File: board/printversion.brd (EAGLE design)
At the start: 70.3 x 34.5 mm, 36 parts, among them IC1 TPS61070DDC, IC2 MEGA8-P, Q2 16MHz

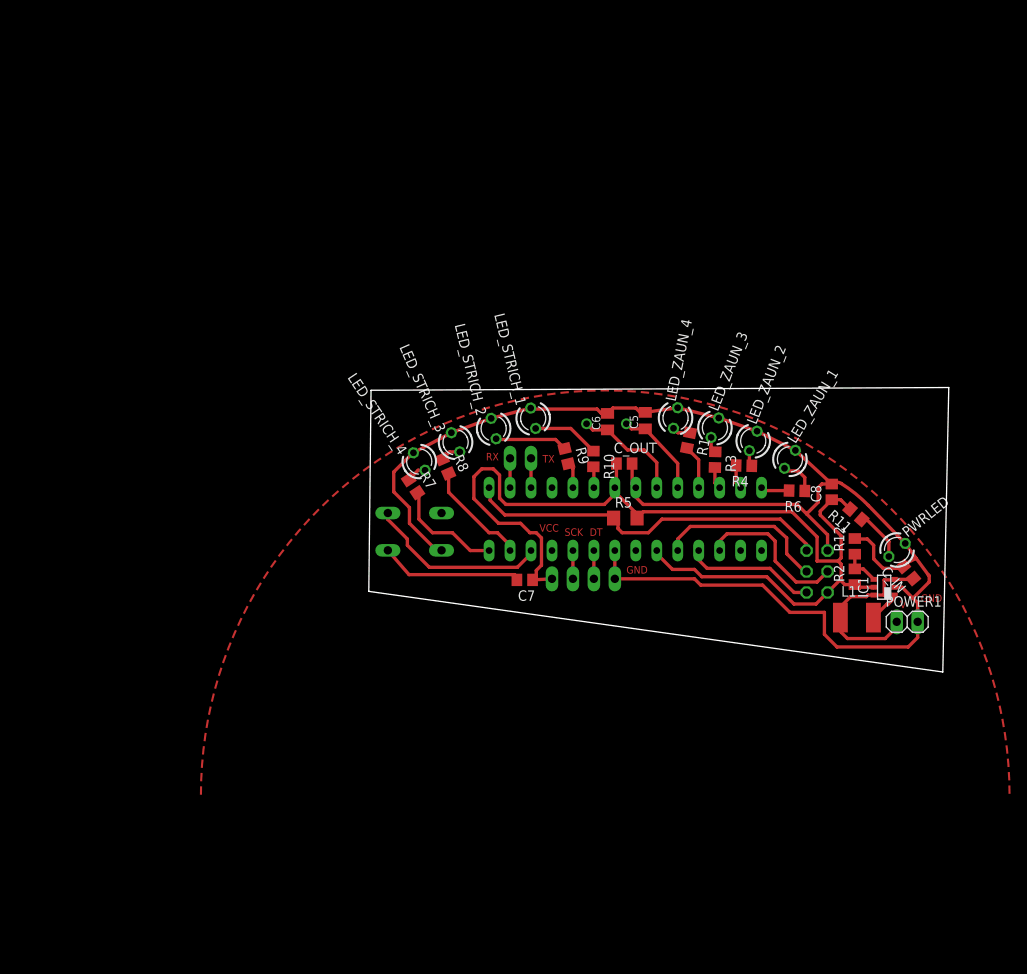
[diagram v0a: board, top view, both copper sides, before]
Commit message: added printversion with multiple boards per page
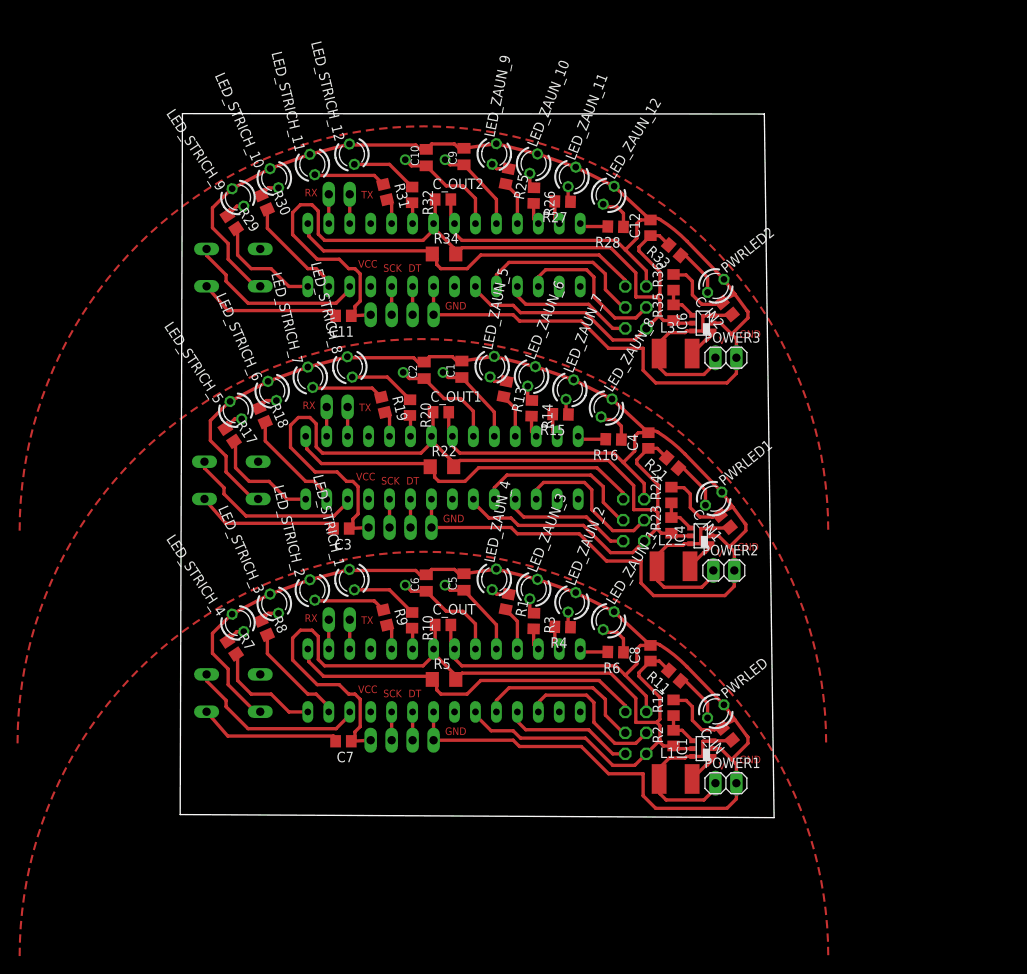
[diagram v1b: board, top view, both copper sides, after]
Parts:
- added C1, C10, C2, C9: 18pF, resistor:C0805K
- added C11, C3: 1uF, rcl-2:C0805
- added C12, C4: 100n, rcl-2:C0805
- added C_IN1, C_IN2, C_OUT1, C_OUT2: (no value), rcl-2:C0805
- added HX2, HX3: JP1, pinhead:1X04
- added IC3, IC5: MEGA8-P, atmel:DIL28-3
- added IC4, IC6: TPS61070DDC, texas:TSOT23-6_DDC
- added ISP2, ISP3: ISP-Connector, con-panduit:057-006-1
- added L2, L3: (no value), rcl:L4532P
- added LED_STRICH_10, LED_STRICH_11, LED_STRICH_12, LED_STRICH_5, LED_STRICH_6, LED_STRICH_7, LED_STRICH_8, LED_STRICH_9, LED_ZAUN_10, LED_ZAUN_11, LED_ZAUN_12, LED_ZAUN_5, LED_ZAUN_6, LED_ZAUN_7, LED_ZAUN_8, LED_ZAUN_9, PWRLED1, PWRLED2: (no value), led:LED3MM
- added POWER2, POWER3, UART2, UART3: JP2, pinhead:1X02
- added Q1, Q3: 16MHz, crystal:HC49/S
- added R13, R14, R15, R16, R17, R18, R19, R20, R21, R25, R26, R27, R28, R29, R30, R31, R32, R33: 470, resistor:R0805
- added R22, R34: 10k, rcl-2:R1206
- added R23, R24, R35, R36: (no value), resistor:R0805
- added S1, S3: S1, switch-omron:B3F-10XX
- moved C6 29.4 mm to (27.3, 25.7)
- moved C7 29.4 mm to (17.3, 6.48)
- moved IC1 29.4 mm to (60.8, 5.59)
- moved IC2 29.4 mm to (29.5, 13.8)
- moved ISP1 29.4 mm to (52.7, 7.49)
- moved PWRLED 29.4 mm to (62.4, 10.1)
- moved R11 29.4 mm to (57.4, 14.4)
- moved R12 29.4 mm to (57.3, 10.5)
- moved R2 29.4 mm to (57.3, 6.86)
- moved R5 29.4 mm to (29.5, 14.0)
- moved R8 29.4 mm to (7.67, 20.2)
- moved C5 29.4 mm to (31.9, 25.8)
- moved C8 29.4 mm to (54.5, 17.1)
- moved LED_STRICH_1 29.4 mm to (18.3, 26.1)
- moved LED_STRICH_3 29.4 mm to (8.89, 23.2)
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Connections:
- new net +5V1: C3.1, C4.1, C_OUT1.1, HX2.4, IC3.20, IC3.7, IC4.5, ISP2.2, R21.2, R22.2, R23.1
- new net +5V2: C11.1, C12.1, C_OUT2.1, HX3.4, IC5.20, IC5.7, IC6.5, ISP3.2, R33.2, R34.2, R35.1
- new net GND1: C1.2, C2.2, C4.2, C_IN1.2, C_OUT1.2, HX2.1, IC3.22, IC3.8, IC4.2, ISP2.6, LED_STRICH_5.K, LED_STRICH_6.K, LED_STRICH_7.K, LED_STRICH_8.K, LED_ZAUN_5.K, LED_ZAUN_6.K, LED_ZAUN_7.K, LED_ZAUN_8.K, POWER2.2, PWRLED1.K, R24.2, S1.3
- new net GND2: C10.2, C12.2, C9.2, C_IN2.2, C_OUT2.2, HX3.1, IC5.22, IC5.8, IC6.2, ISP3.6, LED_STRICH_10.K, LED_STRICH_11.K, LED_STRICH_12.K, LED_STRICH_9.K, LED_ZAUN_10.K, LED_ZAUN_11.K, LED_ZAUN_12.K, LED_ZAUN_9.K, POWER3.2, PWRLED2.K, R36.2, S3.3
- new net N$16: LED_ZAUN_5.A, R13.1
- new net N$17: LED_ZAUN_6.A, R14.1
- new net N$18: LED_ZAUN_7.A, R15.1
- new net N$19: LED_ZAUN_8.A, R16.1
- new net N$20: LED_STRICH_5.A, R17.1
- new net N$21: LED_STRICH_6.A, R18.1
- new net N$22: LED_STRICH_7.A, R19.1
- new net N$23: LED_STRICH_8.A, R20.1
- new net N$24: PWRLED1.A, R21.1
- new net N$25: C1.1, IC3.10, Q1.2
- new net N$26: C2.1, IC3.9, Q1.1
- new net N$27: C3.2, S1.4
- new net N$28: IC4.1, L2.2
- new net N$29: IC4.4, R23.2, R24.1
- new net N$31: LED_ZAUN_9.A, R25.1
- new net N$32: LED_ZAUN_10.A, R26.1
- new net N$33: LED_ZAUN_11.A, R27.1
- new net N$34: LED_ZAUN_12.A, R28.1
- new net N$35: LED_STRICH_9.A, R29.1
- new net N$36: LED_STRICH_10.A, R30.1
- new net N$37: LED_STRICH_11.A, R31.1
- new net N$38: LED_STRICH_12.A, R32.1
- new net N$39: PWRLED2.A, R33.1
- new net N$40: C9.1, IC5.10, Q3.2
- new net N$41: C10.1, IC5.9, Q3.1
- new net N$42: C11.2, S3.4
- new net N$43: IC6.1, L3.2
- new net N$44: IC6.4, R35.2, R36.1
- new net PB0/LED_ZAUN_2: IC3.14, R16.2
- new net PB0/LED_ZAUN_3: IC5.14, R28.2
- new net PB3: IC3.16
- new net PB3/MOSI1: IC3.17, ISP2.4
- new net PB3/MOSI2: IC5.17, ISP3.4
- new net PB4: IC3.15
- new net PB4/MISO1: IC3.18, ISP2.1
- new net PB4/MISO2: IC5.18, ISP3.1
- new net PB5: IC5.16
- new net PB5/SCK1: IC3.19, ISP2.3
- new net PB5/SCK2: IC5.19, ISP3.3
- new net PB6: IC5.15
- new net PC0/DT1: HX2.2, IC3.23
- new net PC0/DT2: HX3.2, IC5.23
- new net PC1: IC3.25
- new net PC1/SCK1: HX2.3, IC3.24
- new net PC1/SCK2: HX3.3, IC5.24
- new net PC4: IC3.26, S1.2
- new net PC4/LED_STRICH_1: IC3.27, R18.2
- new net PC4/LED_STRICH_2: IC5.27, R30.2
- new net PC5: IC5.25
- new net PC5/LED_STRICH_1: IC3.28, R17.2
- new net PC5/LED_STRICH_2: IC5.28, R29.2
- new net PC6: IC5.26, S3.2
- new net PD0/RXD1: IC3.2, UART2.1
- new net PD0/RXD2: IC5.2, UART3.1
- new net PD1: IC3.4
- new net PD1/TXD1: IC3.3, UART2.2
- new net PD1/TXD2: IC5.3, UART3.2
- new net PD3: IC5.4
- new net PD3/LED_STRICH_1: IC3.5, R19.2
- new net PD3/LED_STRICH_3: IC5.5, R31.2
- new net PD4/LED_STRICH_2: IC3.6, R20.2
- new net PD4/LED_STRICH_3: IC5.6, R32.2
- new net PD5/LED_ZAUN_1: IC3.11, R13.2
- new net PD5/LED_ZAUN_2: IC5.11, R25.2
- new net PD6/LED_ZAUN_1: IC3.12, R14.2
- new net PD6/LED_ZAUN_2: IC5.12, R26.2
- new net PD7/LED_ZAUN_1: IC3.13, R15.2
- new net PD7/LED_ZAUN_3: IC5.13, R27.2
- new net RESET1: IC3.1, ISP2.5, R22.1
- new net RESET2: IC5.1, ISP3.5, R34.1
- new net VDD1: IC3.21
- new net VDD2: IC5.21
- new net V_IN1: C_IN1.1, IC4.3, IC4.6, L2.1, POWER2.1
- new net V_IN2: C_IN2.1, IC6.3, IC6.6, L3.1, POWER3.1
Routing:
- net GND1: track 0.00 -> 192.3 mm
- net GND2: track 0.00 -> 192.3 mm
- net +5V1: track 0.00 -> 124.4 mm
- net +5V2: track 0.00 -> 124.4 mm
- net N$45: track 0.00 -> 98.0 mm
- net N$30: track 0.00 -> 98.0 mm
- net RESET2: track 0.00 -> 44.7 mm
- net RESET1: track 0.00 -> 44.7 mm
- net V_IN2: track 0.00 -> 23.0 mm
- net V_IN1: track 0.00 -> 23.0 mm
- net PC4: track 0.00 -> 22.0 mm
- net PC6: track 0.00 -> 22.0 mm
- net PB5/SCK2: track 0.00 -> 21.0 mm
- net PB5/SCK1: track 0.00 -> 21.0 mm
- net PB3/MOSI2: track 0.00 -> 19.0 mm
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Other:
- board size 70.3 x 34.5 mm -> 72 x 85.3 mm
